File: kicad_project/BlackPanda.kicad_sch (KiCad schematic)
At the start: 92 parts, among them J1 Conn_01x04_Female, J2 USB_A TE Connectivity 292303-7, P1 USB-C-USB-3.2-rescue_USB_C_Pl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, Q1 DDTA143ECA-7-F P08, Q2 DDTA143ECA-7-F P08, Q3 PDTC114EU, Q4 HY12P03C2, SW1 SW_Push, U1 AP22615AWU-7, U10 TJA1042TK-3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

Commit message: inductor
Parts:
- removed R5: 442K, Resistor_SMD:R_0402_1005Metric, symbol Device:R_Small
- removed R6: 90.9R, Resistor_SMD:R_0402_1005Metric, symbol Device:R_Small
- L1: value 470NH -> 27nH
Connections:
- net GND: now also R7.2; no longer R7.1
- net at U5.4 (RT/CLK): now also R7.1; no longer R7.2
- no-connect marks 22 -> 23
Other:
- moved on the sheet: R7

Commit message: ...
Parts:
- L1: value 27nH -> 470nH
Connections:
- net GND: no longer J2.5 (Shield)
- no-connect marks 23 -> 24
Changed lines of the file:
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@@
   (junction (at 452.12 287.02) (diameter 0) (color 0 0 0 0)
   )
-  (junction (at 242.57 63.5) (diameter 0) (color 0 0 0 0)
-  )
   (junction (at 184.15 135.89) (diameter 0) (color 0 0 0 0)
   )
@@
   (no_connect (at 344.17 288.29))
   (no_connect (at 344.17 290.83))
+  (no_connect (at 245.11 60.96))
   (no_connect (at 344.17 270.51))
   (no_connect (at 344.17 273.05))
@@
     (stroke (width 0) (type default) (color 0 0 0 0))
   )
-  (wire (pts (xy 242.57 63.5) (xy 245.11 63.5))
+  (wire (pts (xy 240.03 63.5) (xy 245.11 63.5))
     (stroke (width 0) (type default) (color 0 0 0 0))
   )
@@
     (stroke (width 0) (type default) (color 0 0 0 0))
   )
-  (wire (pts (xy 242.57 60.96) (xy 242.57 63.5))
-    (stroke (width 0) (type default) (color 0 0 0 0))
-  )
   (wire (pts (xy 452.12 287.02) (xy 452.12 288.29))
     (stroke (width 0) (type default) (color 0 0 0 0))
@@
     (stroke (width 0) (type default) (color 0 0 0 0))
   )
-  (wire (pts (xy 240.03 63.5) (xy 242.57 63.5))
-    (stroke (width 0) (type default) (color 0 0 0 0))
-  )
   (wire (pts (xy 161.29 116.84) (xy 161.29 115.57))
     (stroke (width 0) (type default) (color 0 0 0 0))
@@
     (stroke (width 0) (type default) (color 0 0 0 0))
   )
-  (wire (pts (xy 245.11 60.96) (xy 242.57 60.96))
-    (stroke (width 0) (type default) (color 0 0 0 0))
-  )
   (wire (pts (xy 443.23 67.31) (xy 443.23 99.06))
     (stroke (width 0) (type default) (color 0 0 0 0))
@@
       (effects (font (size 1.27 1.27)) (justify left))
     )
-    (property "Value" "27nH" (id 1) (at 179.07 314.96 90)
+    (property "Value" "470nH" (id 1) (at 179.07 314.96 90)
       (effects (font (size 1.27 1.27)) (justify left))
     )
@@
     )
     (path "/c49181a2-fbf6-4b90-86bc-374e197edae8"
-      (reference "L1") (unit 1) (value "27nH") (footprint "Inductor_SMD:L_0603_1608Metric")
+      (reference "L1") (unit 1) (value "470nH") (footprint "Inductor_SMD:L_0603_1608Metric")
     )
     (path "/68670b30-42a6-4b81-9cd2-3075b007d192"

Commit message: ...
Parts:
- L1: value 470nH -> 47nH
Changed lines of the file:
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@@
       (effects (font (size 1.27 1.27)) (justify left))
     )
-    (property "Value" "470nH" (id 1) (at 179.07 314.96 90)
+    (property "Value" "47nH" (id 1) (at 179.07 314.96 90)
       (effects (font (size 1.27 1.27)) (justify left))
     )
@@
     )
     (path "/c49181a2-fbf6-4b90-86bc-374e197edae8"
-      (reference "L1") (unit 1) (value "470nH") (footprint "Inductor_SMD:L_0603_1608Metric")
+      (reference "L1") (unit 1) (value "47nH") (footprint "Inductor_SMD:L_0603_1608Metric")
     )
     (path "/68670b30-42a6-4b81-9cd2-3075b007d192"

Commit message: ...
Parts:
- C15: value 100NF -> 10NF
- L1: value 47nH -> 27nH
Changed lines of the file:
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@@
       (effects (font (size 1.27 1.27)) (justify left))
     )
-    (property "Value" "100NF" (id 1) (at 182.88 293.37 90)
+    (property "Value" "10NF" (id 1) (at 182.88 293.37 90)
       (effects (font (size 1.27 1.27)) (justify left))
     )
@@
       (effects (font (size 1.27 1.27)) (justify left))
     )
-    (property "Value" "47nH" (id 1) (at 179.07 314.96 90)
+    (property "Value" "27nH" (id 1) (at 179.07 314.96 90)
       (effects (font (size 1.27 1.27)) (justify left))
     )
@@
     )
     (path "/0fa36f25-46e1-4a71-8956-7acf510e5ef2"
-      (reference "C15") (unit 1) (value "100NF") (footprint "Capacitor_SMD:C_0402_1005Metric")
+      (reference "C15") (unit 1) (value "10NF") (footprint "Capacitor_SMD:C_0402_1005Metric")
     )
     (path "/5772887d-ec8f-4cc7-973c-928fb373308f"
@@
     )
     (path "/c49181a2-fbf6-4b90-86bc-374e197edae8"
-      (reference "L1") (unit 1) (value "47nH") (footprint "Inductor_SMD:L_0603_1608Metric")
+      (reference "L1") (unit 1) (value "27nH") (footprint "Inductor_SMD:L_0603_1608Metric")
     )
     (path "/68670b30-42a6-4b81-9cd2-3075b007d192"

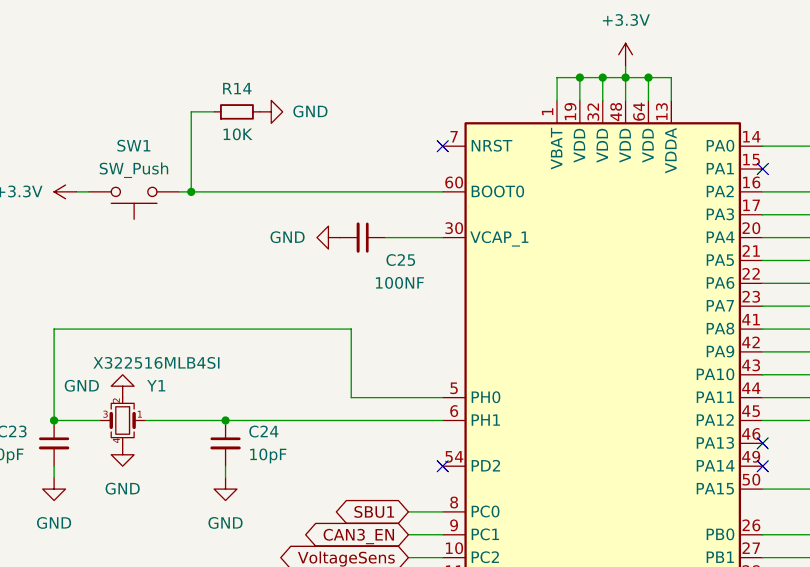
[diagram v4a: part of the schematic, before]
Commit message: Capacitor incorrect value.
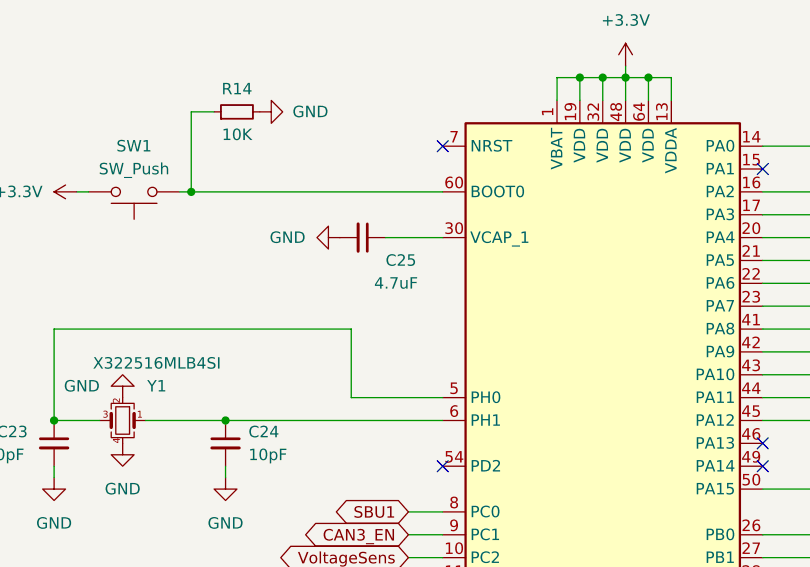
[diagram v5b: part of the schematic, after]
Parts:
- C25: value 100NF -> 4.7uF
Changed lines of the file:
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@@
       (effects (font (size 1.27 1.27)) (justify left))
     )
-    (property "Value" "100NF" (id 1) (at 300.99 252.73 90)
+    (property "Value" "4.7uF" (id 1) (at 300.99 252.73 90)
       (effects (font (size 1.27 1.27)) (justify left))
     )
@@
     )
     (path "/4236d0f6-8821-4c7c-a0a6-efc7b018fe64"
-      (reference "C25") (unit 1) (value "100NF") (footprint "Capacitor_SMD:C_0402_1005Metric")
+      (reference "C25") (unit 1) (value "4.7uF") (footprint "Capacitor_SMD:C_0402_1005Metric")
     )
     (path "/3dfd07fd-4fbf-4e5a-b40f-fa678140a611"
